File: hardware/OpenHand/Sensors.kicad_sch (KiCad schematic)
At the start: 0 parts

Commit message: Minor comment update
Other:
- note added: "How to power EMG sensor circuit (split rail)"
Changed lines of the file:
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@@
     (fill (type none))
+  )
+  (text "How to power EMG sensor circuit (split rail)" (at 27.94 45.72 0)
+    (effects (font (size 1.27 1.27) (thickness 0.254) bold) (justify left bottom))
   )
   (text "EMG SENSOR" (at 25.4 30.48 0)

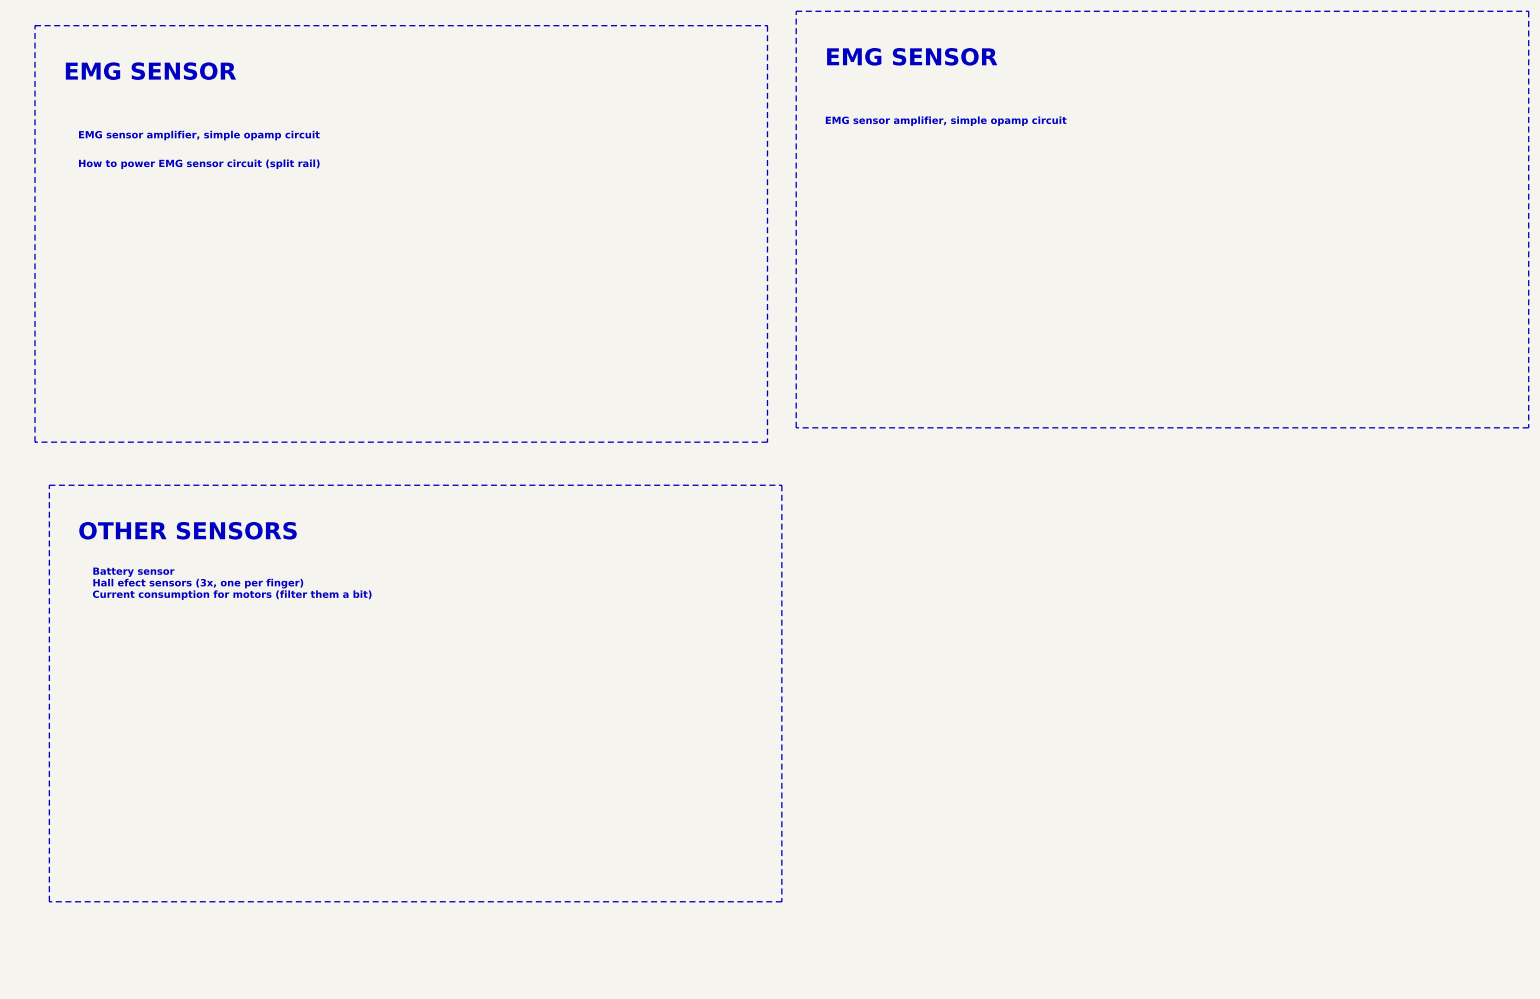
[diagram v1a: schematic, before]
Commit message: Started adding ICs to schematic
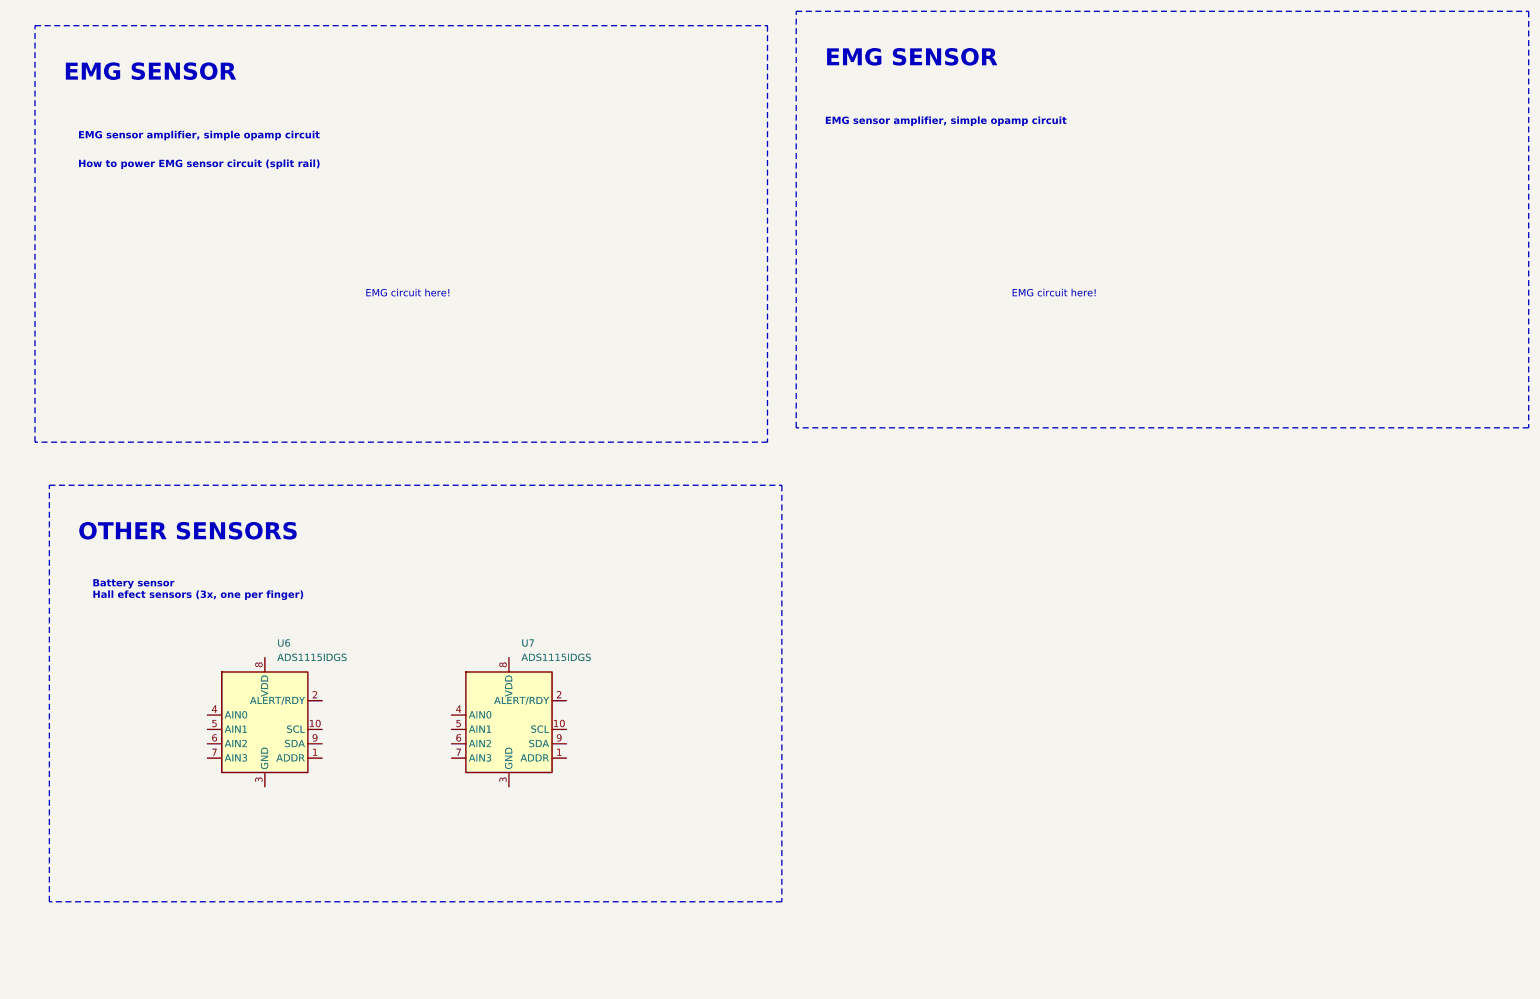
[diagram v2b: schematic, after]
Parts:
- added U6, U7: ADS1115IDGS, Package_SO:TSSOP-10_3x3mm_P0.5mm, symbol Analog_ADC:ADS1115IDGS
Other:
- note added: "Battery sensor Hall efect sensors (3x, one per finger)"
- note added: "EMG circuit here!"
- note removed: "Battery sensor Hall efect sensors (3x, one per finger) Current consumption for motors (filter them a bit)"
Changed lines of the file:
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@@
     (effects (font (size 3 3) (thickness 0.6) bold) (justify left bottom))
+  )
+  (text "EMG circuit here!" (at 193.04 68.58 0)
+    (effects (font (size 1.27 1.27)) (justify left bottom) (href "https://www.instructables.com/Muscle-EMG-Sensor-for-a-Microcontroller/"))
+  )
+  (text "EMG circuit here!" (at 78.74 68.58 0)
+    (effects (font (size 1.27 1.27)) (justify left bottom) (href "https://www.instructables.com/Muscle-EMG-Sensor-for-a-Microcontroller/"))
   )
   (text "EMG sensor amplifier, simple opamp circuit" (at 27.94 40.64 0)
     (effects (font (size 1.27 1.27) bold) (justify left bottom))
   )
-  (text "Battery sensor\nHall efect sensors (3x, one per finger)\nCurrent consumption for motors (filter them a bit)"
+  (text "Battery sensor\nHall efect sensors (3x, one per finger)"
     (at 30.48 121.92 0)
     (effects (font (size 1.27 1.27) bold) (justify left bottom))
   )
+  (symbol (lib_id "Analog_ADC:ADS1115IDGS") (at 60.96 144.78 0) (unit 1)
+    (in_bom yes) (on_board yes) (dnp no) (fields_autoplaced)
+    (property "Reference" "U6" (at 63.1541 129.54 0)
+      (effects (font (size 1.27 1.27)) (justify left))
+    )
+    (property "Value" "ADS1115IDGS" (at 63.1541 132.08 0)
+      (effects (font (size 1.27 1.27)) (justify left))
+    )
+    (property "Footprint" "Package_SO:TSSOP-10_3x3mm_P0.5mm" (at 60.96 157.48 0)
+      (effects (font (size 1.27 1.27)) hide)
+    )
+    (property "Datasheet" "http://www.ti.com/lit/ds/symlink/ads1113.pdf" (at 59.69 167.64 0)
+      (effects (font (size 1.27 1.27)) hide)
+    )
+    (pin "1")
+    (pin "10")
+    (pin "2")
+    (pin "3")
+    (pin "4")
+    (pin "5")
+    (pin "6")
+    (pin "7")
+    (pin "8")
+    (pin "9")
+    (instances
+      (project "OpenHand"
+        (path "/f1fbd835-8408-4592-854c-2fbec9d052ec/286dde41-8068-419e-b7de-6276970410d8"
+          (reference "U6") (unit 1)
+        )
+      )
+    )
+  )
+  (symbol (lib_id "Analog_ADC:ADS1115IDGS") (at 104.14 144.78 0) (unit 1)
+    (in_bom yes) (on_board yes) (dnp no) (fields_autoplaced)
+    (property "Reference" "U7" (at 106.3341 129.54 0)
+      (effects (font (size 1.27 1.27)) (justify left))
+    )
+    (property "Value" "ADS1115IDGS" (at 106.3341 132.08 0)
+      (effects (font (size 1.27 1.27)) (justify left))
+    )
+    (property "Footprint" "Package_SO:TSSOP-10_3x3mm_P0.5mm" (at 104.14 157.48 0)
+      (effects (font (size 1.27 1.27)) hide)
+    )
+    (property "Datasheet" "http://www.ti.com/lit/ds/symlink/ads1113.pdf" (at 102.87 167.64 0)
+      (effects (font (size 1.27 1.27)) hide)
+    )
+    (pin "1")
+    (pin "10")
+    (pin "2")
+    (pin "3")
+    (pin "4")
+    (pin "5")
+    (pin "6")
+    (pin "7")
+    (pin "8")
+    (pin "9")
+    (instances
+      (project "OpenHand"
+        (path "/f1fbd835-8408-4592-854c-2fbec9d052ec/286dde41-8068-419e-b7de-6276970410d8"
+          (reference "U7") (unit 1)
+        )
+      )
+    )
+  )
 )

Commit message: Update schematic
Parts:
- added U10, U9: OPA333xxDBV, Package_TO_SOT_SMD:SOT-23-5, symbol Amplifier_Operational:OPA333xxDBV
- added U8: INA333xxDGK, Package_SO:VSSOP-8_3.0x3.0mm_P0.65mm, symbol Amplifier_Instrumentation:INA333xxDGK
- renumbered U6 to U3, U7 to U4
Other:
- note removed: "EMG circuit here!"
- note removed: "EMG sensor amplifier, simple opamp circuit"
- note removed: "How to power EMG sensor circuit (split rail)"
- moved on the sheet: U3, U4
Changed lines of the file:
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@@
 (kicad_sch (version 20230121) (generator eeschema)
   (paper "A4")
-  (rectangle (start 154.94 17.78) (end 284.48 91.44)
+  (rectangle (start 152.4 17.78) (end 279.4 104.14)
     (stroke (width 0) (type dash_dot))
     (fill (type none))
   )
-  (rectangle (start 20.32 20.32) (end 149.86 93.98)
+  (rectangle (start 17.78 17.78) (end 144.78 104.14)
     (stroke (width 0) (type dash_dot))
     (fill (type none))
   )
-  (rectangle (start 22.86 101.6) (end 152.4 175.26)
+  (rectangle (start 17.78 116.84) (end 147.32 190.5)
     (stroke (width 0) (type dash_dot))
     (fill (type none))
   )
-  (text "How to power EMG sensor circuit (split rail)" (at 27.94 45.72 0)
-    (effects (font (size 1.27 1.27) (thickness 0.254) bold) (justify left bottom))
-  )
-  (text "EMG SENSOR" (at 25.4 30.48 0)
+  (text "EMG SENSOR" (at 20.32 25.4 0)
     (effects (font (size 3 3) (thickness 0.6) bold) (justify left bottom))
   )
-  (text "EMG SENSOR" (at 160.02 27.94 0)
+  (text "EMG SENSOR" (at 154.94 25.4 0)
     (effects (font (size 3 3) (thickness 0.6) bold) (justify left bottom))
   )
-  (text "EMG sensor amplifier, simple opamp circuit" (at 160.02 38.1 0)
+  (text "OTHER SENSORS" (at 22.86 127 0)
+    (effects (font (size 3 3) (thickness 0.6) bold) (justify left bottom))
+  )
+  (text "Battery sensor\nHall efect sensors (3x, one per finger)"
+    (at 25.4 137.16 0)
     (effects (font (size 1.27 1.27) bold) (justify left bottom))
   )
-  (text "OTHER SENSORS" (at 27.94 111.76 0)
-    (effects (font (size 3 3) (thickness 0.6) bold) (justify left bottom))
+  (symbol (lib_id "Amplifier_Instrumentation:INA333xxDGK") (at 73.66 53.34 0) (unit 1)
+    (in_bom yes) (on_board yes) (dnp no) (fields_autoplaced)
+    (property "Reference" "U8" (at 88.9 49.1491 0)
+      (effects (font (size 1.27 1.27)))
+    )
+    (property "Value" "INA333xxDGK" (at 88.9 51.6891 0)
+      (effects (font (size 1.27 1.27)))
+    )
+    (property "Footprint" "Package_SO:VSSOP-8_3.0x3.0mm_P0.65mm" (at 73.66 60.96 0)
+      (effects (font (size 1.27 1.27)) hide)
+    )
+    (property "Datasheet" "https://www.ti.com/lit/ds/symlink/ina333.pdf" (at 76.2 53.34 0)
+      (effects (font (size 1.27 1.27)) hide)
+    )
+    (pin "1")
+    (pin "2")
+    (pin "3")
+    (pin "4")
+    (pin "5")
+    (pin "6")
+    (pin "7")
+    (pin "8")
+    (instances
+      (project "OpenHand"
+        (path "/f1fbd835-8408-4592-854c-2fbec9d052ec/286dde41-8068-419e-b7de-6276970410d8"
+          (reference "U8") (unit 1)
+        )
+      )
+    )
   )
-  (text "EMG circuit here!" (at 193.04 68.58 0)
-    (effects (font (size 1.27 1.27)) (justify left bottom) (href "https://www.instructables.com/Muscle-EMG-Sensor-for-a-Microcontroller/"))
-  )
-  (text "EMG circuit here!" (at 78.74 68.58 0)
-    (effects (font (size 1.27 1.27)) (justify left bottom) (href "https://www.instructables.com/Muscle-EMG-Sensor-for-a-Microcontroller/"))
-  )
-  (text "EMG sensor amplifier, simple opamp circuit" (at 27.94 40.64 0)
-    (effects (font (size 1.27 1.27) bold) (justify left bottom))
-  )
-  (text "Battery sensor\nHall efect sensors (3x, one per finger)"
-    (at 30.48 121.92 0)
-    (effects (font (size 1.27 1.27) bold) (justify left bottom))
-  )
-  (symbol (lib_id "Analog_ADC:ADS1115IDGS") (at 60.96 144.78 0) (unit 1)
+  (symbol (lib_id "Analog_ADC:ADS1115IDGS") (at 55.88 160.02 0) (unit 1)
     (in_bom yes) (on_board yes) (dnp no) (fields_autoplaced)
-    (property "Reference" "U6" (at 63.1541 129.54 0)
+    (property "Reference" "U3" (at 58.0741 144.78 0)
       (effects (font (size 1.27 1.27)) (justify left))
     )
-    (property "Value" "ADS1115IDGS" (at 63.1541 132.08 0)
+    (property "Value" "ADS1115IDGS" (at 58.0741 147.32 0)
       (effects (font (size 1.27 1.27)) (justify left))
     )
-    (property "Footprint" "Package_SO:TSSOP-10_3x3mm_P0.5mm" (at 60.96 157.48 0)
+    (property "Footprint" "Package_SO:TSSOP-10_3x3mm_P0.5mm" (at 55.88 172.72 0)
       (effects (font (size 1.27 1.27)) hide)
     )
-    (property "Datasheet" "http://www.ti.com/lit/ds/symlink/ads1113.pdf" (at 59.69 167.64 0)
+    (property "Datasheet" "http://www.ti.com/lit/ds/symlink/ads1113.pdf" (at 54.61 182.88 0)
       (effects (font (size 1.27 1.27)) hide)
     )
@@
       (project "OpenHand"
         (path "/f1fbd835-8408-4592-854c-2fbec9d052ec/286dde41-8068-419e-b7de-6276970410d8"
-          (reference "U6") (unit 1)
+          (reference "U3") (unit 1)
         )
       )
     )
   )
-  (symbol (lib_id "Analog_ADC:ADS1115IDGS") (at 104.14 144.78 0) (unit 1)
+  (symbol (lib_id "Analog_ADC:ADS1115IDGS") (at 99.06 160.02 0) (unit 1)
     (in_bom yes) (on_board yes) (dnp no) (fields_autoplaced)
-    (property "Reference" "U7" (at 106.3341 129.54 0)
+    (property "Reference" "U4" (at 101.2541 144.78 0)
       (effects (font (size 1.27 1.27)) (justify left))
     )
-    (property "Value" "ADS1115IDGS" (at 106.3341 132.08 0)
+    (property "Value" "ADS1115IDGS" (at 101.2541 147.32 0)
       (effects (font (size 1.27 1.27)) (justify left))
     )
-    (property "Footprint" "Package_SO:TSSOP-10_3x3mm_P0.5mm" (at 104.14 157.48 0)
+    (property "Footprint" "Package_SO:TSSOP-10_3x3mm_P0.5mm" (at 99.06 172.72 0)
       (effects (font (size 1.27 1.27)) hide)
     )
-    (property "Datasheet" "http://www.ti.com/lit/ds/symlink/ads1113.pdf" (at 102.87 167.64 0)
+    (property "Datasheet" "http://www.ti.com/lit/ds/symlink/ads1113.pdf" (at 97.79 182.88 0)
       (effects (font (size 1.27 1.27)) hide)
     )
@@
       (project "OpenHand"
         (path "/f1fbd835-8408-4592-854c-2fbec9d052ec/286dde41-8068-419e-b7de-6276970410d8"
-          (reference "U7") (unit 1)
+          (reference "U4") (unit 1)
         )
       )
+    )
+  )
+  (symbol (lib_id "Amplifier_Operational:OPA333xxDBV") (at 73.66 78.74 0) (unit 1)
+    (in_bom yes) (on_board yes) (dnp no) (fields_autoplaced)
+    (property "Reference" "U9" (at 86.36 74.5491 0)
+      (effects (font (size 1.27 1.27)))
+    )
+    (property "Value" "OPA333xxDBV" (at 86.36 77.0891 0)
+      (effects (font (size 1.27 1.27)))
+    )
+    (property "Footprint" "Package_TO_SOT_SMD:SOT-23-5" (at 71.12 83.82 0)
+      (effects (font (size 1.27 1.27)) (justify left) hide)
+    )
+    (property "Datasheet" "http://www.ti.com/lit/ds/symlink/opa333.pdf" (at 73.66 73.66 0)
+      (effects (font (size 1.27 1.27)) hide)
+    )
+    (pin "2")
+    (pin "5")
+    (pin "1")
+    (pin "3")
+    (pin "4")
+    (instances
+      (project "OpenHand"
+        (path "/f1fbd835-8408-4592-854c-2fbec9d052ec/286dde41-8068-419e-b7de-6276970410d8"
+          (reference "U9") (unit 1)
+        )
+      )
+    )
+  )
+  (symbol (lib_id "Amplifier_Operational:OPA333xxDBV") (at 111.76 55.88 0) (unit 1)
+    (in_bom yes) (on_board yes) (dnp no) (fields_autoplaced)
+    (property "Reference" "U10" (at 124.46 51.6891 0)
+      (effects (font (size 1.27 1.27)))
+    )
+    (property "Value" "OPA333xxDBV" (at 124.46 54.2291 0)
+      (effects (font (size 1.27 1.27)))
+    )
+    (property "Footprint" "Package_TO_SOT_SMD:SOT-23-5" (at 109.22 60.96 0)
+      (effects (font (size 1.27 1.27)) (justify left) hide)
+    )
+    (property "Datasheet" "http://www.ti.com/lit/ds/symlink/opa333.pdf" (at 111.76 50.8 0)
+      (effects (font (size 1.27 1.27)) hide)
+    )
+    (pin "2")
+    (pin "5")
+    (pin "1")
+    (pin "3")
+    (pin "4")
+    (instances
+      (project "OpenHand"
+        (path "/f1fbd835-8408-4592-854c-2fbec9d052ec/286dde41-8068-419e-b7de-6276970410d8"
+          (reference "U10") (unit 1)
+        )
+      )

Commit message: working on schematics
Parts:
- removed U4: ADS1115IDGS, Package_SO:TSSOP-10_3x3mm_P0.5mm, symbol Analog_ADC:ADS1115IDGS
- added R10, R12, R8, R9: 10k, Resistor_SMD:R_1206_3216Metric, symbol Device:R
- added R11: 47k, Resistor_SMD:R_1206_3216Metric, symbol Device:R
- renumbered U8 to U3, U10 to U4, U9 to U5, U3 to U6
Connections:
- net Earth: now reaches U6.1 (ADDR)
- net Earth: now also U6.3 (GND), R12.1
- net UC_SCL: now reaches U6.10 (SCL)
- net UC_SCL: now also R9.1
- net ADC_ALERT_RDY: now reaches U6.2 (ALERT/RDY)
- net ADC_ALERT_RDY: now also R8.1
- net at U6.4 (AIN0): now also R11.1, R12.2
- net HALL_SENS_01_S: now reaches U6.5 (AIN1)
- net HALL_SENS_02_S: now reaches U6.6 (AIN2)
- net HALL_SENS_03_S: now reaches U6.7 (AIN3)
- net +3V3: now reaches U6.8 (VDD)
- net +3V3: now also R10.2, R8.2, R9.2
- net UC_SDA: now reaches U6.9 (SDA)
- net UC_SDA: now also R10.1
- new net BAT_P: R11.2
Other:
- note added: "Battery voltage sensor 3x hall efect sensors (one per finger)"
- note added: "Hall effect sensors supply"
- note added: "I2C pullups"
- note added: "Up to 4 ICs per I2C line, connect ADDR line to ground, VDD, SDA, or SCL to select address"
- note added: "Voltage divider: - max bat voltage 12.6V - gives us ~2.2V on output"
- note removed: "Battery sensor Hall efect sensors (3x, one per finger)"
- title: (none) -> OpenHand prosthetic hand controller project
- moved on the sheet: U6
